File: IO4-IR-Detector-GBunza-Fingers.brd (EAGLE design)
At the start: 12.1 x 45.7 mm, 3 parts

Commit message: 1.0-panel
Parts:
- added J10, J11, J12, J13, J14, J15, J16, J2, J3, J4, J5, J6, J7, J8, J9: (no value), SPCoast:1X04_LOCK
- added T.AMBIENT1, T.AMBIENT10, T.AMBIENT11, T.AMBIENT12, T.AMBIENT13, T.AMBIENT14, T.AMBIENT15, T.AMBIENT2, T.AMBIENT3, T.AMBIENT4, T.AMBIENT5, T.AMBIENT6, T.AMBIENT7, T.AMBIENT8, T.AMBIENT9, T.DETECTED1, T.DETECTED10, T.DETECTED11, T.DETECTED12, T.DETECTED13, T.DETECTED14, T.DETECTED15, T.DETECTED2, T.DETECTED3, T.DETECTED4, T.DETECTED5, T.DETECTED6, T.DETECTED7, T.DETECTED8, T.DETECTED9: PT19-21C/L41, SparkFun-Sensors:ALS-PT19
- moved J1 45.7 mm to (2.41, 47.9)
- moved T.AMBIENT 45.7 mm to (9.27, 51.7)
- moved T.DETECTED 44.5 mm to (6.10, 67.7)
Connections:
- new net N$1: J2.4, T.AMBIENT1.E
- new net N$10: J4.1, T.DETECTED3.E
- new net N$11: J4.2, T.DETECTED3.C
- new net N$12: J4.3, T.AMBIENT3.C
- new net N$17: J5.4, T.AMBIENT4.E
- new net N$18: J5.1, T.DETECTED4.E
- new net N$19: J5.2, T.DETECTED4.C
- new net N$2: J2.1, T.DETECTED1.E
- new net N$20: J5.3, T.AMBIENT4.C
- new net N$21: J6.4, T.AMBIENT5.E
- new net N$22: J6.1, T.DETECTED5.E
- new net N$23: J6.2, T.DETECTED5.C
- new net N$24: J6.3, T.AMBIENT5.C
- new net N$25: J7.4, T.AMBIENT6.E
- new net N$26: J7.1, T.DETECTED6.E
- new net N$27: J7.2, T.DETECTED6.C
- new net N$28: J7.3, T.AMBIENT6.C
- new net N$29: J8.4, T.AMBIENT7.E
- new net N$3: J2.2, T.DETECTED1.C
- new net N$30: J8.1, T.DETECTED7.E
- new net N$31: J8.2, T.DETECTED7.C
- new net N$32: J8.3, T.AMBIENT7.C
- new net N$33: J9.4, T.AMBIENT8.E
- new net N$34: J9.1, T.DETECTED8.E
- new net N$35: J9.2, T.DETECTED8.C
- new net N$36: J9.3, T.AMBIENT8.C
- new net N$37: J10.4, T.AMBIENT9.E
- new net N$38: J10.1, T.DETECTED9.E
- new net N$39: J10.2, T.DETECTED9.C
- new net N$4: J2.3, T.AMBIENT1.C
- new net N$40: J10.3, T.AMBIENT9.C
- new net N$41: J11.4, T.AMBIENT10.E
- new net N$42: J11.1, T.DETECTED10.E
- new net N$43: J11.2, T.DETECTED10.C
- new net N$44: J11.3, T.AMBIENT10.C
- new net N$45: J12.4, T.AMBIENT11.E
- new net N$46: J12.1, T.DETECTED11.E
- new net N$47: J12.2, T.DETECTED11.C
- new net N$48: J12.3, T.AMBIENT11.C
- new net N$49: J13.4, T.AMBIENT12.E
- new net N$5: J3.4, T.AMBIENT2.E
- new net N$50: J13.1, T.DETECTED12.E
- new net N$51: J13.2, T.DETECTED12.C
- new net N$52: J13.3, T.AMBIENT12.C
- new net N$53: J14.4, T.AMBIENT13.E
- new net N$54: J14.1, T.DETECTED13.E
- new net N$55: J14.2, T.DETECTED13.C
- new net N$56: J14.3, T.AMBIENT13.C
- new net N$57: J15.4, T.AMBIENT14.E
- new net N$58: J15.1, T.DETECTED14.E
- new net N$59: J15.2, T.DETECTED14.C
- new net N$6: J3.1, T.DETECTED2.E
- new net N$60: J15.3, T.AMBIENT14.C
- new net N$61: J16.4, T.AMBIENT15.E
- new net N$62: J16.1, T.DETECTED15.E
- new net N$63: J16.2, T.DETECTED15.C
- new net N$64: J16.3, T.AMBIENT15.C
- new net N$7: J3.2, T.DETECTED2.C
- new net N$8: J3.3, T.AMBIENT2.C
- new net N$9: J4.4, T.AMBIENT3.E
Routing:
- net N$51: track 0.00 -> 26.6 mm, vias 0 -> 1
- net N$47: track 0.00 -> 26.6 mm, vias 0 -> 1
- net N$39: track 0.00 -> 26.6 mm, vias 0 -> 1
- net N$3: track 0.00 -> 26.6 mm, vias 0 -> 1
- net N$27: track 0.00 -> 26.6 mm, vias 0 -> 1
- net N$23: track 0.00 -> 26.6 mm, vias 0 -> 1
- net N$11: track 0.00 -> 26.6 mm, vias 0 -> 1
- net N$7: track 0.00 -> 26.6 mm, vias 0 -> 1
- net N$63: track 0.00 -> 26.6 mm, vias 0 -> 1
- net N$55: track 0.00 -> 26.6 mm, vias 0 -> 1
- net N$43: track 0.00 -> 26.6 mm, vias 0 -> 1
- net N$35: track 0.00 -> 26.6 mm, vias 0 -> 1
- net N$19: track 0.00 -> 26.6 mm, vias 0 -> 1
- net N$59: track 0.00 -> 26.6 mm, vias 0 -> 1
- net N$31: track 0.00 -> 26.6 mm, vias 0 -> 1
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- removed copper zone on layer 16, net VCC
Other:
- board size 12.1 x 45.7 mm -> 102.9 x 107.4 mm
- board text added: "2018-01"
- board text added: "IR Detector Fingers"
- board text added: "John Plocher"
- board text added: "Made in the PRC"
- board text added: "Model Railroading is Fun!"
- board text added: "V-SCORE"
- board text added: "v1.0"
- board text added: "www.SPCoast.com"

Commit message: 1.1-panel
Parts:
- moved T.DETECTED1 6.54 mm to (5.97, 30.3)
- moved T.DETECTED11 6.54 mm to (54.2, 30.3)
- moved T.DETECTED12 6.54 mm to (78.4, 30.3)
- moved T.DETECTED14 6.54 mm to (90.4, 30.3)
- moved T.DETECTED3 6.54 mm to (18.0, 30.3)
- moved T.DETECTED5 6.54 mm to (30.1, 30.3)
- moved T.DETECTED6 6.54 mm to (42.2, 30.3)
- moved T.DETECTED9 6.54 mm to (66.3, 30.3)
- moved T.AMBIENT1 5.27 mm to (2.79, 45.0)
- moved T.AMBIENT11 5.27 mm to (51.1, 45.0)
- moved T.AMBIENT12 5.27 mm to (75.2, 45.0)
- moved T.AMBIENT14 5.27 mm to (87.2, 45.0)
- moved T.AMBIENT3 5.27 mm to (14.9, 45.0)
- moved T.AMBIENT5 5.27 mm to (26.9, 45.0)
- moved T.AMBIENT6 5.27 mm to (39.0, 45.0)
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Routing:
- net N$7: track 26.6 -> 24.1 mm
- net N$63: track 26.6 -> 24.1 mm
- net N$55: track 26.6 -> 24.1 mm
- net N$43: track 26.6 -> 24.1 mm
- net N$35: track 26.6 -> 24.1 mm
- net N$31: track 26.6 -> 24.1 mm
- net N$19: track 26.6 -> 24.1 mm
- net N$15: track 26.6 -> 24.1 mm
- net N$59: track 26.6 -> 24.1 mm
- net N$51: track 26.6 -> 24.1 mm
- net N$47: track 26.6 -> 24.1 mm
- net N$39: track 26.6 -> 24.1 mm
- net N$3: track 26.6 -> 24.1 mm
- net N$27: track 26.6 -> 24.1 mm
- net N$23: track 26.6 -> 24.1 mm
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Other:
- board size 102.9 x 107.4 mm -> 103 x 107.4 mm
- board text added: "2018-02"
- board text added: "Made in the PRC, Coast Division, NMRA"
- board text added: "SPCoast.com"
- board text added: "v1.1"
- board text removed: "2018-01"
- board text removed: "Made in the PRC"
- board text removed: "v1.0"

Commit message: added values for connectors
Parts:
- J1, J10, J11, J12, J13, J14, J15, J16, J2, J3, J4, J5, J6, J7, J8, J9: value (none) -> 0.100
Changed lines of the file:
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@@
 <grid distance="50" unitdist="mil" unit="mil" style="dots" multiple="2" display="yes" altdistance="25" altunitdist="mil" altunit="mil"/>
 <layers>
-<layer number="1" name="Top" color="4" fill="1" visible="no" active="yes"/>
-<layer number="16" name="Bottom" color="2" fill="1" visible="no" active="yes"/>
+<layer number="1" name="Top" color="4" fill="1" visible="yes" active="yes"/>
+<layer number="16" name="Bottom" color="2" fill="1" visible="yes" active="yes"/>
 <layer number="17" name="Pads" color="23" fill="1" visible="yes" active="yes"/>
 <layer number="18" name="Vias" color="29" fill="1" visible="yes" active="yes"/>
-<layer number="19" name="Unrouted" color="6" fill="1" visible="no" active="yes"/>
+<layer number="19" name="Unrouted" color="6" fill="1" visible="yes" active="yes"/>
 <layer number="20" name="Dimension" color="15" fill="1" visible="yes" active="yes"/>
 <layer number="21" name="tPlace" color="19" fill="1" visible="yes" active="yes"/>
 <layer number="22" name="bPlace" color="17" fill="1" visible="no" active="yes"/>
-<layer number="23" name="tOrigins" color="30" fill="1" visible="no" active="yes"/>
+<layer number="23" name="tOrigins" color="30" fill="1" visible="yes" active="yes"/>
 <layer number="24" name="bOrigins" color="15" fill="1" visible="no" active="yes"/>
-<layer number="25" name="tNames" color="63" fill="1" visible="no" active="yes"/>
+<layer number="25" name="tNames" color="63" fill="1" visible="yes" active="yes"/>
 <layer number="26" name="bNames" color="34" fill="1" visible="no" active="yes"/>
 <layer number="27" name="tValues" color="56" fill="1" visible="yes" active="yes"/>
@@
 <layer number="42" name="bRestrict" color="3" fill="10" visible="no" active="yes"/>
 <layer number="43" name="vRestrict" color="2" fill="10" visible="no" active="yes"/>
-<layer number="44" name="Drills" color="16" fill="1" visible="no" active="yes"/>
-<layer number="45" name="Holes" color="35" fill="1" visible="no" active="yes"/>
+<layer number="44" name="Drills" color="16" fill="1" visible="yes" active="yes"/>
+<layer number="45" name="Holes" color="35" fill="1" visible="yes" active="yes"/>
 <layer number="46" name="Milling" color="35" fill="1" visible="yes" active="yes"/>
-<layer number="47" name="Measures" color="21" fill="1" visible="no" active="yes"/>
+<layer number="47" name="Measures" color="21" fill="1" visible="yes" active="yes"/>
 <layer number="48" name="Document" color="24" fill="1" visible="yes" active="yes"/>
-<layer number="49" name="Reference" color="48" fill="1" visible="no" active="yes"/>
+<layer number="49" name="Reference" color="48" fill="1" visible="yes" active="yes"/>
 <layer number="50" name="dxf" color="7" fill="1" visible="no" active="yes"/>
 <layer number="51" name="tDocu" color="24" fill="1" visible="yes" active="yes"/>
@@
 <attribute name="PROD_ID" value="IC-11836" x="6.096" y="69.151" size="1.778" layer="27" rot="R270" display="off"/>
 </element>
-<element name="J1" library="SPCoast" package="1X04_LOCK" value="" x="2.413" y="51.879" smashed="yes">
+<element name="J1" library="SPCoast" package="1X04_LOCK" value="0.100" x="2.413" y="51.879" smashed="yes">
 <attribute name="VALUE" x="1.143" y="48.704" size="1.27" layer="27"/>
 </element>
@@
 <attribute name="PROD_ID" value="IC-11836" x="5.969" y="30.289" size="1.778" layer="27" rot="R90" display="off"/>
 </element>
-<element name="J2" library="SPCoast" package="1X04_LOCK" value="" x="9.652" y="47.561" smashed="yes" rot="R180">
+<element name="J2" library="SPCoast" package="1X04_LOCK" value="0.100" x="9.652" y="47.561" smashed="yes" rot="R180">
 <attribute name="VALUE" x="10.922" y="50.736" size="1.27" layer="27" rot="R180"/>
 </element>
@@
 <attribute name="PROD_ID" value="IC-11836" x="18.161" y="69.151" size="1.778" layer="27" rot="R270" display="off"/>
 </element>
-<element name="J3" library="SPCoast" package="1X04_LOCK" value="" x="14.478" y="51.879" smashed="yes">
+<element name="J3" library="SPCoast" package="1X04_LOCK" value="0.100" x="14.478" y="51.879" smashed="yes">
 <attribute name="VALUE" x="13.208" y="48.704" size="1.27" layer="27"/>
 </element>
@@
 <attribute name="PROD_ID" value="IC-11836" x="18.034" y="30.289" size="1.778" layer="27" rot="R90" display="off"/>
 </element>
-<element name="J4" library="SPCoast" package="1X04_LOCK" value="" x="21.717" y="47.561" smashed="yes" rot="R180">
+<element name="J4" library="SPCoast" package="1X04_LOCK" value="0.100" x="21.717" y="47.561" smashed="yes" rot="R180">
 <attribute name="VALUE" x="22.987" y="50.736" size="1.27" layer="27" rot="R180"/>
 </element>
@@
 <attribute name="PROD_ID" value="IC-11836" x="30.226" y="69.151" size="1.778" layer="27" rot="R270" display="off"/>
 </element>
-<element name="J5" library="SPCoast" package="1X04_LOCK" value="" x="26.543" y="51.879" smashed="yes">
+<element name="J5" library="SPCoast" package="1X04_LOCK" value="0.100" x="26.543" y="51.879" smashed="yes">
 <attribute name="VALUE" x="25.273" y="48.704" size="1.27" layer="27"/>
 </element>
@@
 <attribute name="PROD_ID" value="IC-11836" x="30.099" y="30.289" size="1.778" layer="27" rot="R90" display="off"/>
 </element>
-<element name="J6" library="SPCoast" package="1X04_LOCK" value="" x="33.782" y="47.561" smashed="yes" rot="R180">
+<element name="J6" library="SPCoast" package="1X04_LOCK" value="0.100" x="33.782" y="47.561" smashed="yes" rot="R180">
 <attribute name="VALUE" x="35.052" y="50.736" size="1.27" layer="27" rot="R180"/>
 </element>
@@
 <attribute name="PROD_ID" value="IC-11836" x="42.164" y="30.289" size="1.778" layer="27" rot="R90" display="off"/>
 </element>
-<element name="J7" library="SPCoast" package="1X04_LOCK" value="" x="45.847" y="47.561" smashed="yes" rot="R180">
+<element name="J7" library="SPCoast" package="1X04_LOCK" value="0.100" x="45.847" y="47.561" smashed="yes" rot="R180">
 <attribute name="VALUE" x="47.117" y="50.736" size="1.27" layer="27" rot="R180"/>
 </element>
@@
 <attribute name="PROD_ID" value="IC-11836" x="42.291" y="69.151" size="1.778" layer="27" rot="R270" display="off"/>
 </element>
-<element name="J8" library="SPCoast" package="1X04_LOCK" value="" x="38.608" y="51.879" smashed="yes">
+<element name="J8" library="SPCoast" package="1X04_LOCK" value="0.100" x="38.608" y="51.879" smashed="yes">
 <attribute name="VALUE" x="37.338" y="48.704" size="1.27" layer="27"/>
 </element>
@@
 <attribute name="PROD_ID" value="IC-11836" x="66.421" y="69.151" size="1.778" layer="27" rot="R270" display="off"/>
 </element>
-<element name="J9" library="SPCoast" package="1X04_LOCK" value="" x="62.738" y="51.879" smashed="yes">
+<element name="J9" library="SPCoast" package="1X04_LOCK" value="0.100" x="62.738" y="51.879" smashed="yes">
 <attribute name="VALUE" x="61.468" y="48.704" size="1.27" layer="27"/>
 </element>
@@
 <attribute name="PROD_ID" value="IC-11836" x="66.294" y="30.289" size="1.778" layer="27" rot="R90" display="off"/>
 </element>
-<element name="J10" library="SPCoast" package="1X04_LOCK" value="" x="69.977" y="47.561" smashed="yes" rot="R180">
+<element name="J10" library="SPCoast" package="1X04_LOCK" value="0.100" x="69.977" y="47.561" smashed="yes" rot="R180">
 <attribute name="VALUE" x="71.247" y="50.736" size="1.27" layer="27" rot="R180"/>
 </element>
@@
 <attribute name="PROD_ID" value="IC-11836" x="54.356" y="69.151" size="1.778" layer="27" rot="R270" display="off"/>
 </element>
-<element name="J11" library="SPCoast" package="1X04_LOCK" value="" x="50.673" y="51.879" smashed="yes">
+<element name="J11" library="SPCoast" package="1X04_LOCK" value="0.100" x="50.673" y="51.879" smashed="yes">
 <attribute name="VALUE" x="49.403" y="48.704" size="1.27" layer="27"/>
 </element>
@@
 <attribute name="PROD_ID" value="IC-11836" x="54.229" y="30.289" size="1.778" layer="27" rot="R90" display="off"/>
 </element>
-<element name="J12" library="SPCoast" package="1X04_LOCK" value="" x="57.912" y="47.561" smashed="yes" rot="R180">
+<element name="J12" library="SPCoast" package="1X04_LOCK" value="0.100" x="57.912" y="47.561" smashed="yes" rot="R180">
 <attribute name="VALUE" x="59.182" y="50.736" size="1.27" layer="27" rot="R180"/>
 </element>
@@
 <attribute name="PROD_ID" value="IC-11836" x="78.359" y="30.289" size="1.778" layer="27" rot="R90" display="off"/>
 </element>
-<element name="J13" library="SPCoast" package="1X04_LOCK" value="" x="82.042" y="47.561" smashed="yes" rot="R180">
+<element name="J13" library="SPCoast" package="1X04_LOCK" value="0.100" x="82.042" y="47.561" smashed="yes" rot="R180">
 <attribute name="VALUE" x="83.312" y="50.736" size="1.27" layer="27" rot="R180"/>
 </element>
@@
 <attribute name="PROD_ID" value="IC-11836" x="78.486" y="69.151" size="1.778" layer="27" rot="R270" display="off"/>
 </element>
-<element name="J14" library="SPCoast" package="1X04_LOCK" value="" x="74.803" y="51.879" smashed="yes">
+<element name="J14" library="SPCoast" package="1X04_LOCK" value="0.100" x="74.803" y="51.879" smashed="yes">
 <attribute name="VALUE" x="73.533" y="48.704" size="1.27" layer="27"/>
 </element>
@@
 <attribute name="PROD_ID" value="IC-11836" x="90.424" y="30.289" size="1.778" layer="27" rot="R90" display="off"/>
 </element>
-<element name="J15" library="SPCoast" package="1X04_LOCK" value="" x="94.107" y="47.561" smashed="yes" rot="R180">
+<element name="J15" library="SPCoast" package="1X04_LOCK" value="0.100" x="94.107" y="47.561" smashed="yes" rot="R180">
 <attribute name="VALUE" x="95.377" y="50.736" size="1.27" layer="27" rot="R180"/>
 </element>
@@
 <attribute name="PROD_ID" value="IC-11836" x="90.551" y="69.151" size="1.778" layer="27" rot="R270" display="off"/>
 </element>
-<element name="J16" library="SPCoast" package="1X04_LOCK" value="" x="86.868" y="51.879" smashed="yes">
+<element name="J16" library="SPCoast" package="1X04_LOCK" value="0.100" x="86.868" y="51.879" smashed="yes">
 <attribute name="VALUE" x="85.598" y="48.704" size="1.27" layer="27"/>
 </element>

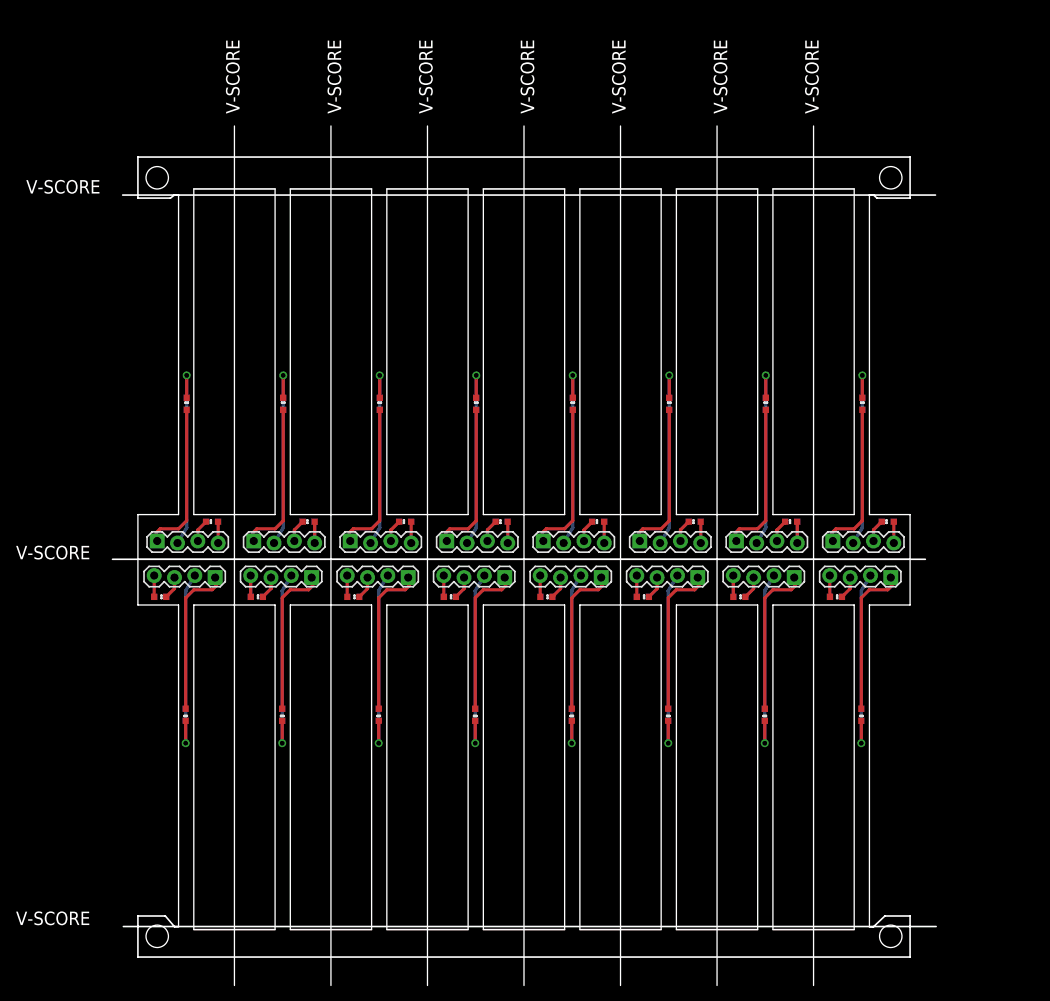
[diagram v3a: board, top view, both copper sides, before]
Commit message: replace vscore w/mouse bites, enlarge for fab
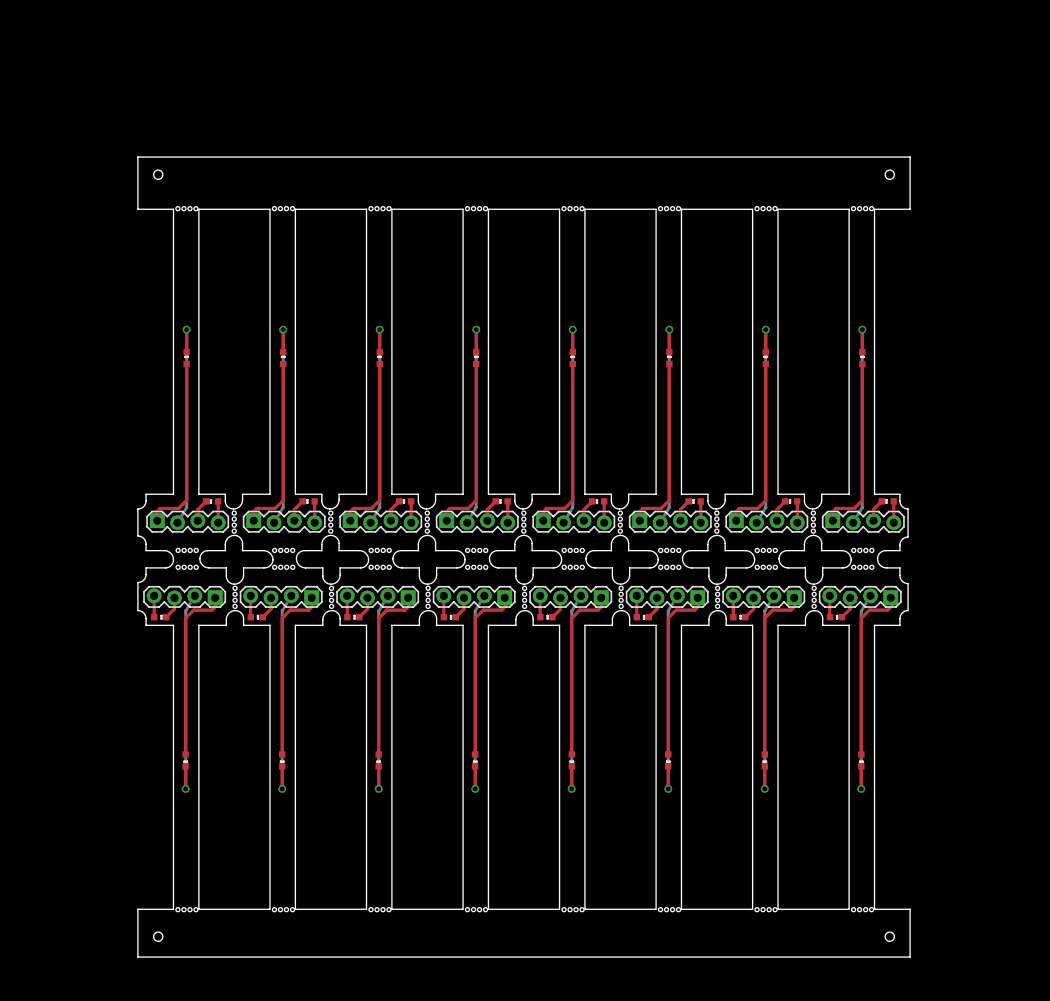
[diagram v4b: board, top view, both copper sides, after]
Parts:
- added U$1, U$2, U$3, U$4: (no value), SPCoast:MOUNTINGHOLE-TOOL
- moved T.DETECTED 5.72 mm to (6.10, 74.9)
- moved T.DETECTED10 5.72 mm to (54.4, 74.9)
- moved T.DETECTED13 5.72 mm to (78.5, 74.9)
- moved T.DETECTED15 5.72 mm to (90.6, 74.9)
- moved T.DETECTED2 5.72 mm to (18.2, 74.9)
- moved T.DETECTED4 5.72 mm to (30.2, 74.9)
- moved T.DETECTED7 5.72 mm to (42.3, 74.9)
- moved T.DETECTED8 5.72 mm to (66.4, 74.9)
- moved T.DETECTED1 5.71 mm to (5.97, 24.6)
- moved T.DETECTED11 5.71 mm to (54.2, 24.6)
- moved T.DETECTED12 5.71 mm to (78.4, 24.6)
- moved T.DETECTED14 5.71 mm to (90.4, 24.6)
- moved T.DETECTED3 5.71 mm to (18.0, 24.6)
- moved T.DETECTED5 5.71 mm to (30.1, 24.6)
- moved T.DETECTED6 5.71 mm to (42.2, 24.6)
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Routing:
- net N$7: track 24.1 -> 27.3 mm
- net N$63: track 24.1 -> 27.3 mm
- net N$62: track 19.3 -> 22.5 mm
- net N$6: track 19.3 -> 22.5 mm
- net N$55: track 24.1 -> 27.3 mm
- net N$54: track 19.3 -> 22.5 mm
- net N$43: track 24.1 -> 27.3 mm
- net N$42: track 19.3 -> 22.5 mm
- net N$35: track 24.1 -> 27.3 mm
- net N$34: track 19.3 -> 22.5 mm
- net N$31: track 24.1 -> 27.3 mm
- net N$30: track 19.3 -> 22.5 mm
- net N$19: track 24.1 -> 27.3 mm
- net N$18: track 19.3 -> 22.5 mm
- net N$15: track 24.1 -> 27.3 mm
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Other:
- board size 103 x 107.4 mm -> 96.5 x 100 mm
- board text added: "For GBunza Detector"
- board text added: "JLCJLCJLCJLC"
- board text added: "v1.2 2022.03"
- board text removed: "V-SCORE"
- board text removed: "v1.1"
